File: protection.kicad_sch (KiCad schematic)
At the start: 11 parts

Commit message: Correct part LCSC codes and values
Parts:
- F701: value 1206T4A63V -> 12T.40000063AG12S1B02; LCSC C354899 -> C140479
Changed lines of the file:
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@@
     (in_bom yes) (on_board yes)
     (property "Reference" "F701" (id 0) (at 43.18 48.3362 90))
-    (property "Value" "1206T4A63V" (id 1) (at 43.18 50.6476 90))
+    (property "Value" "12T.40000063AG12S1B02" (id 1) (at 43.18 50.6476 90))
     (property "Footprint" "Fuse:Fuse_1206_3216Metric" (id 2) (at 43.18 51.562 90)
       (effects (font (size 1.27 1.27)) hide)
@@
       (effects (font (size 1.27 1.27)) hide)
     )
-    (property "LCSC" "C354899" (id 4) (at 43.18 53.34 90)
+    (property "LCSC" "C140479" (id 4) (at 43.18 53.34 90)
       (effects (font (size 1.27 1.27)) hide)
     )

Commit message: Move rotation definitions to component fields
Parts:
- D702: value SS5U100 -> 10S45SP; LCSC C698774 -> C2988031
- L701: value CMF7060F-701-2P-T -> PCAQ7060MW-102; LCSC C2998446 -> C2915648

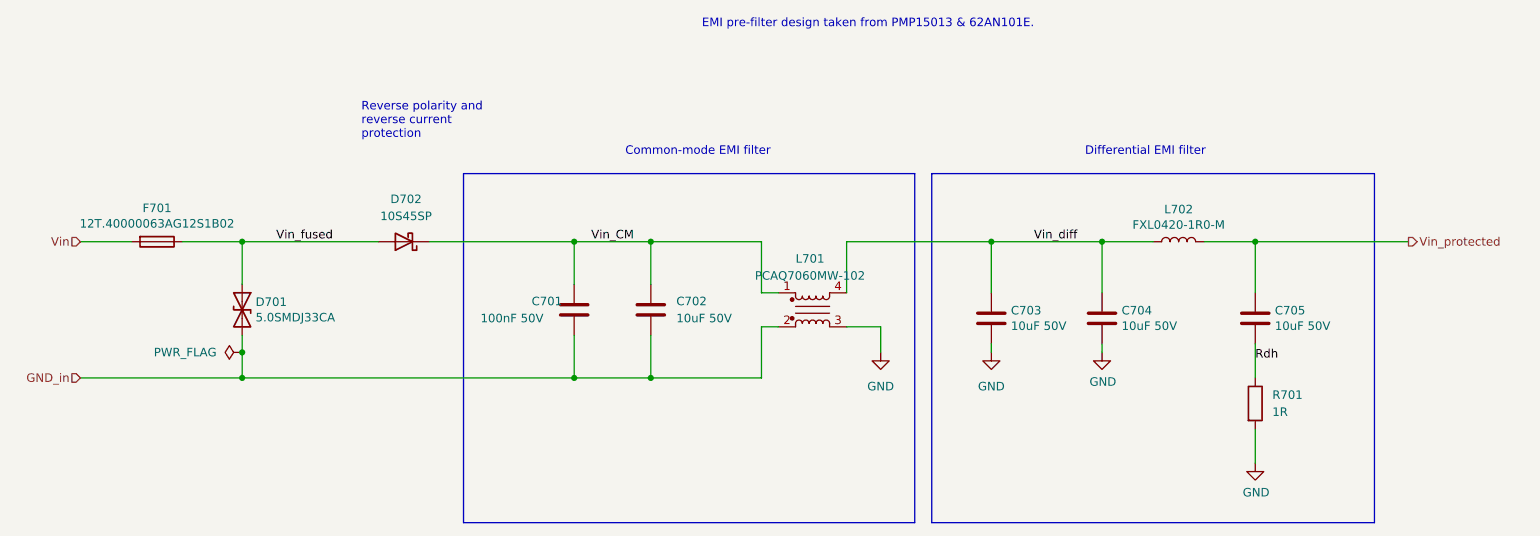
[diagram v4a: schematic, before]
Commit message: Rename power input sheets
Also tweak pass-through connector solder paste margins.
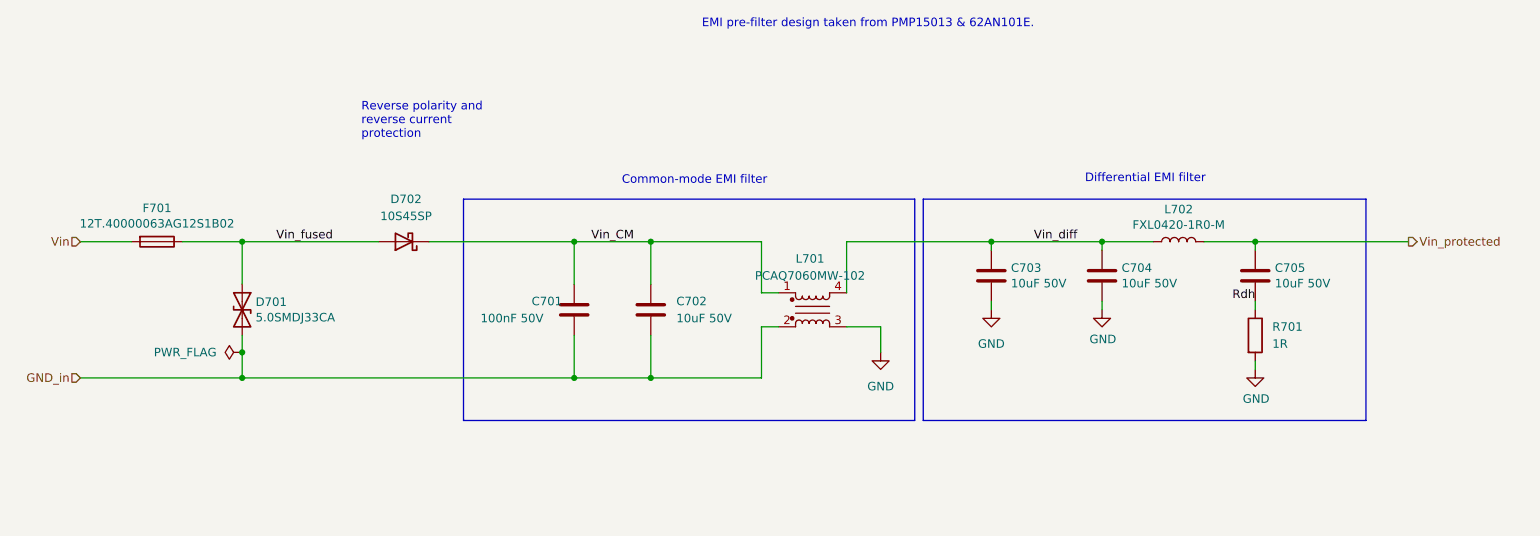
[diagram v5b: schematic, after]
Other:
- moved on the sheet: C703, C704, C705, R701
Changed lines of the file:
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@@
 	(polyline
 		(pts
-			(xy 158.75 43.18) (xy 224.79 43.18)
-		)
-		(stroke
-			(width 0)
-			(type default)
-		)
-	)
-	(wire
-		(pts
-			(xy 207.01 68.58) (xy 207.01 73.66)
-		)
-		(stroke
-			(width 0)
-			(type default)
-		)
-	)
-	(wire
-		(pts
-			(xy 184.15 60.96) (xy 184.15 53.34)
+			(xy 157.48 46.99) (xy 223.52 46.99)
+		)
+		(stroke
+			(width 0)
+			(type default)
+		)
+	)
+	(wire
+		(pts
+			(xy 207.01 62.23) (xy 207.01 63.5)
+		)
+		(stroke
+			(width 0)
+			(type default)
+		)
+	)
+	(wire
+		(pts
+			(xy 184.15 54.61) (xy 184.15 53.34)
 		)
 		(stroke
@@
 	(wire
 		(pts
-			(xy 207.01 60.96) (xy 207.01 53.34)
+			(xy 207.01 54.61) (xy 207.01 53.34)
 		)
 		(stroke
@@
 	(polyline
 		(pts
-			(xy 158.75 43.18) (xy 158.75 95.25)
+			(xy 157.48 46.99) (xy 157.48 80.01)
 		)
 		(stroke
@@
 	(polyline
 		(pts
-			(xy 224.79 43.18) (xy 224.79 95.25)
+			(xy 223.52 46.99) (xy 223.52 80.01)
 		)
 		(stroke
@@
 	(wire
 		(pts
-			(xy 167.64 68.58) (xy 167.64 69.85)
+			(xy 167.64 62.23) (xy 167.64 63.5)
 		)
 		(stroke
@@
 	(wire
 		(pts
-			(xy 207.01 81.28) (xy 207.01 86.36)
+			(xy 207.01 71.12) (xy 207.01 72.39)
 		)
 		(stroke
@@
 	(polyline
 		(pts
-			(xy 224.79 95.25) (xy 158.75 95.25)
+			(xy 223.52 80.01) (xy 157.48 80.01)
 		)
 		(stroke
@@
 	(polyline
 		(pts
-			(xy 156.21 43.18) (xy 156.21 95.25)
+			(xy 156.21 46.99) (xy 156.21 80.01)
 		)
 		(stroke
@@
 	(polyline
 		(pts
-			(xy 156.21 43.18) (xy 88.9 43.18)
+			(xy 156.21 46.99) (xy 88.9 46.99)
 		)
 		(stroke
@@
 	(wire
 		(pts
-			(xy 167.64 53.34) (xy 167.64 60.96)
+			(xy 167.64 53.34) (xy 167.64 54.61)
 		)
 		(stroke
@@
 	(wire
 		(pts
-			(xy 184.15 68.58) (xy 184.15 69.85)
+			(xy 184.15 62.23) (xy 184.15 63.5)
 		)
 		(stroke
@@
 	(polyline
 		(pts
-			(xy 88.9 43.18) (xy 88.9 95.25)
+			(xy 88.9 46.99) (xy 88.9 80.01)
 		)
 		(stroke
@@
 	(polyline
 		(pts
-			(xy 88.9 95.25) (xy 156.21 95.25)
+			(xy 88.9 80.01) (xy 156.21 80.01)
 		)
 		(stroke
@@
 	(text "Differential EMI filter"
 		(exclude_from_sim no)
-		(at 181.61 40.64 0)
+		(at 181.61 44.704 0)
 		(effects
 			(font
@@
 	(text "Common-mode EMI filter"
 		(exclude_from_sim no)
-		(at 113.03 40.64 0)
+		(at 112.522 44.958 0)
 		(effects
 			(font
@@
 	)
 	(label "Rdh"
-		(at 207.01 71.12 0)
+		(at 207.01 62.23 180)
 		(fields_autoplaced yes)
 		(effects
@@
 				(size 1.27 1.27)
 			)
-			(justify left bottom)
+			(justify right bottom)
 		)
 	)
@@
 	(symbol
 		(lib_id "Device:C")
-		(at 184.15 64.77 0)
+		(at 184.15 58.42 0)
 		(unit 1)
 		(exclude_from_sim no)
@@
 		(dnp no)
 		(property "Reference" "C704"
-			(at 187.071 63.6016 0)
+			(at 187.071 57.2516 0)
 			(effects
 				(font
@@
 		)
 		(property "Value" "10uF 50V"
-			(at 187.071 65.913 0)
+			(at 187.071 59.563 0)
 			(effects
 				(font
@@
 		)
 		(property "Footprint" "Capacitor_SMD:C_1206_3216Metric"
-			(at 185.1152 68.58 0)
+			(at 185.1152 62.23 0)
 			(effects
 				(font
@@
 		)
 		(property "Datasheet" "~"
-			(at 184.15 64.77 0)
+			(at 184.15 58.42 0)
 			(effects
 				(font
@@
 		)
 		(property "Description" ""
-			(at 184.15 64.77 0)
+			(at 184.15 58.42 0)
 			(effects
 				(font
@@
 		)
 		(property "LCSC" "C13585"
-			(at 184.15 64.77 0)
+			(at 184.15 58.42 0)
 			(effects
 				(font
@@
 	(symbol
 		(lib_id "power:GND")
-		(at 184.15 69.85 0)
+		(at 184.15 63.5 0)
 		(unit 1)
 		(exclude_from_sim no)
@@
 		(dnp no)
 		(property "Reference" "#PWR0703"
-			(at 184.15 76.2 0)
+			(at 184.15 69.85 0)
 			(effects
 				(font
@@
 		)
 		(property "Value" "GND"
-			(at 184.277 74.2442 0)
+			(at 184.277 67.8942 0)
 			(effects
 				(font
@@
 		)
 		(property "Footprint" ""
-			(at 184.15 69.85 0)
+			(at 184.15 63.5 0)
 			(effects
 				(font
@@
 		)
 		(property "Datasheet" ""
-			(at 184.15 69.85 0)
+			(at 184.15 63.5 0)
 			(effects
 				(font
@@
 		)
 		(property "Description" ""
-			(at 184.15 69.85 0)
+			(at 184.15 63.5 0)
 			(effects
 				(font
@@
 	(symbol
 		(lib_id "Device:C")
-		(at 207.01 64.77 0)
+		(at 207.01 58.42 0)
 		(unit 1)
 		(exclude_from_sim no)
@@
 		(dnp no)
 		(property "Reference" "C705"
-			(at 209.931 63.6016 0)
+			(at 209.931 57.2516 0)
 			(effects
 				(font
@@
 		)
 		(property "Value" "10uF 50V"
-			(at 209.931 65.913 0)
+			(at 209.931 59.563 0)
 			(effects
 				(font
@@
 		)
 		(property "Footprint" "Capacitor_SMD:C_1206_3216Metric"
-			(at 207.9752 68.58 0)
+			(at 207.9752 62.23 0)
 			(effects
 				(font
@@
 		)
 		(property "Datasheet" "~"
-			(at 207.01 64.77 0)
+			(at 207.01 58.42 0)
 			(effects
 				(font
@@
 		)
 		(property "Description" ""
-			(at 207.01 64.77 0)
+			(at 207.01 58.42 0)
 			(effects
 				(font
@@
 		)
 		(property "LCSC" "C13585"
-			(at 207.01 64.77 0)
+			(at 207.01 58.42 0)
 			(effects
 				(font
@@
 	(symbol
 		(lib_id "power:GND")
-		(at 207.01 86.36 0)
+		(at 207.01 72.39 0)
 		(unit 1)
 		(exclude_from_sim no)
@@
 		(dnp no)
 		(property "Reference" "#PWR0704"
-			(at 207.01 92.71 0)
+			(at 207.01 78.74 0)
 			(effects
 				(font
@@
 		)
 		(property "Value" "GND"
-			(at 207.137 90.7542 0)
+			(at 207.137 76.7842 0)
 			(effects
 				(font
@@
 		)
 		(property "Footprint" ""
-			(at 207.01 86.36 0)
+			(at 207.01 72.39 0)
 			(effects
 				(font
@@
 		)
 		(property "Datasheet" ""
-			(at 207.01 86.36 0)
+			(at 207.01 72.39 0)
 			(effects
 				(font
@@
 		)
 		(property "Description" ""
-			(at 207.01 86.36 0)
+			(at 207.01 72.39 0)
 			(effects
 				(font
@@
 	(symbol
 		(lib_id "Device:R")
-		(at 207.01 77.47 0)
+		(at 207.01 67.31 0)
 		(unit 1)
 		(exclude_from_sim no)
@@
 		(fields_autoplaced yes)
 		(property "Reference" "R701"
-			(at 209.55 76.1999 0)
+			(at 209.55 66.0399 0)
 			(effects
 				(font
@@
 		)
 		(property "Value" "1R"
-			(at 209.55 78.7399 0)
+			(at 209.55 68.5799 0)
 			(effects
 				(font
@@
 		)
 		(property "Footprint" "Capacitor_SMD:C_0603_1608Metric"
-			(at 205.232 77.47 90)
+			(at 205.232 67.31 90)
 			(effects
 				(font
@@
 		)
 		(property "Datasheet" "~"
-			(at 207.01 77.47 0)
+			(at 207.01 67.31 0)
 			(effects
 				(font
@@
 		)
 		(property "Description" ""
-			(at 207.01 77.47 0)
+			(at 207.01 67.31 0)
 			(effects
 				(font
@@
 		)
 		(property "LCSC" "C22936"
-			(at 207.01 77.47 0)
+			(at 207.01 67.31 0)
 			(effects
 				(font
@@
 	(symbol
 		(lib_id "Device:C")
-		(at 167.64 64.77 0)
+		(at 167.64 58.42 0)
 		(unit 1)
 		(exclude_from_sim no)
@@
 		(dnp no)
 		(property "Reference" "C703"
-			(at 170.561 63.6016 0)
+			(at 170.561 57.2516 0)
 			(effects
 				(font
@@
 		)
 		(property "Value" "10uF 50V"
-			(at 170.561 65.913 0)
+			(at 170.561 59.563 0)
 			(effects
 				(font
@@
 		)
 		(property "Footprint" "Capacitor_SMD:C_1206_3216Metric"
-			(at 168.6052 68.58 0)
+			(at 168.6052 62.23 0)
 			(effects
 				(font
@@
 		)
 		(property "Datasheet" "~"
-			(at 167.64 64.77 0)
+			(at 167.64 58.42 0)
 			(effects
 				(font
@@
 		)
 		(property "Description" ""
-			(at 167.64 64.77 0)
+			(at 167.64 58.42 0)
 			(effects
 				(font
@@
 		)
 		(property "LCSC" "C13585"
-			(at 167.64 64.77 0)
+			(at 167.64 58.42 0)
 			(effects
 				(font
@@
 	(symbol
 		(lib_id "power:GND")
-		(at 167.64 69.85 0)
+		(at 167.64 63.5 0)
 		(unit 1)
 		(exclude_from_sim no)
@@
 		(fields_autoplaced yes)
 		(property "Reference" "#PWR0702"
-			(at 167.64 76.2 0)
+			(at 167.64 69.85 0)
 			(effects
 				(font
@@
 		)
 		(property "Value" "GND"
-			(at 167.64 74.93 0)
+			(at 167.64 68.58 0)
 			(effects
 				(font
@@
 		)
 		(property "Footprint" ""
-			(at 167.64 69.85 0)
+			(at 167.64 63.5 0)
 			(effects
 				(font
@@
 		)
 		(property "Datasheet" ""
-			(at 167.64 69.85 0)
+			(at 167.64 63.5 0)
 			(effects
 				(font
@@
 		)
 		(property "Description" ""
-			(at 167.64 69.85 0)
-			(effects
-				(font
+			(at 167.64 63.5 0)
+			(effects
+				(font
